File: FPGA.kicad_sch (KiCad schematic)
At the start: 14 parts, among them U3 XC7A100T-FTG256, U5 S25FL127S

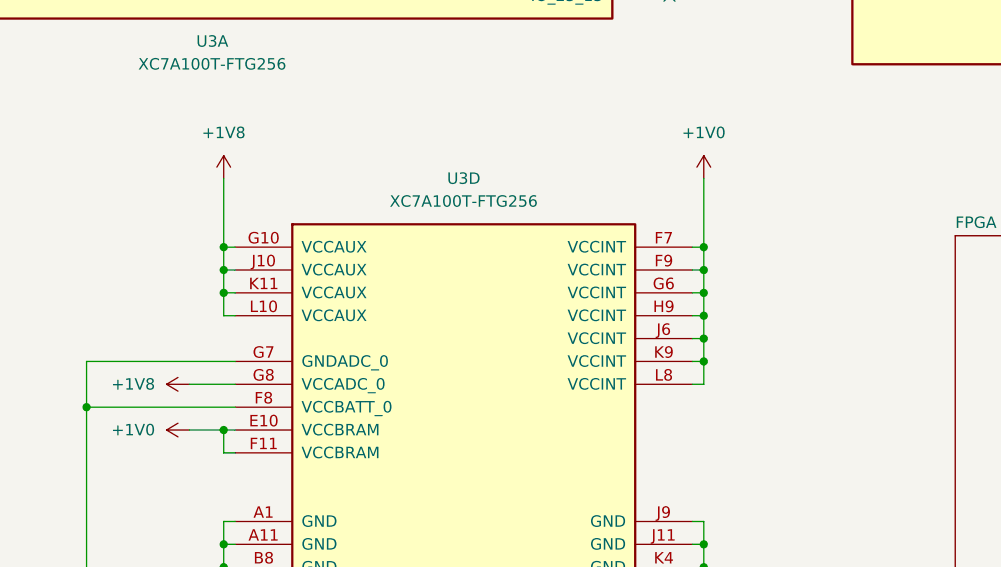
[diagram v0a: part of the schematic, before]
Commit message: Resolved some Electrial Rules
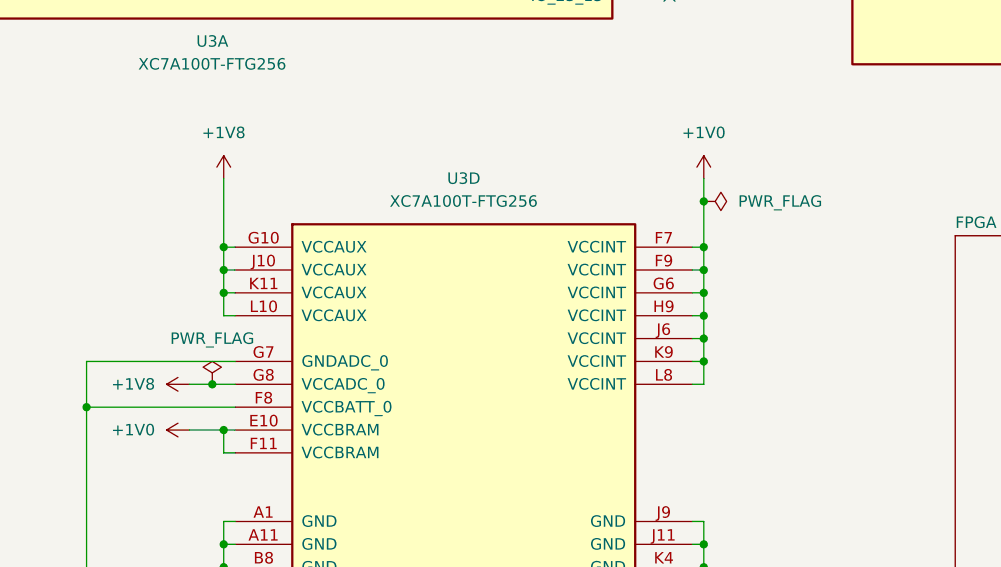
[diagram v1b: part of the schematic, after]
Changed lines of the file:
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@@
   (junction (at 236.22 204.47) (diameter 0) (color 0 0 0 0)
   )
+  (junction (at 289.56 196.85) (diameter 0) (color 0 0 0 0)
+  )
   (junction (at 109.22 182.88) (diameter 0) (color 0 0 0 0)
   )
@@
   )
   (junction (at 236.22 237.49) (diameter 0) (color 0 0 0 0)
+  )
+  (junction (at 234.95 217.17) (diameter 0) (color 0 0 0 0)
   )
   (junction (at 312.42 29.21) (diameter 0) (color 0 0 0 0)
@@
     (stroke (width 0) (type default))
   )
+  (wire (pts (xy 289.56 196.85) (xy 289.56 201.93))
+    (stroke (width 0) (type default))
+  )
   (wire (pts (xy 66.04 78.74) (xy 66.04 81.28))
     (stroke (width 0) (type default))
@@
     (stroke (width 0) (type default))
   )
+  (wire (pts (xy 234.95 217.17) (xy 237.49 217.17))
+    (stroke (width 0) (type default))
+  )
   (wire (pts (xy 236.22 267.97) (xy 237.49 267.97))
     (stroke (width 0) (type default))
@@
     (stroke (width 0) (type default))
   )
-  (wire (pts (xy 232.41 217.17) (xy 237.49 217.17))
+  (wire (pts (xy 232.41 217.17) (xy 234.95 217.17))
     (stroke (width 0) (type default))
   )
@@
     (stroke (width 0) (type default))
   )
-  (wire (pts (xy 289.56 194.31) (xy 289.56 201.93))
+  (wire (pts (xy 289.56 194.31) (xy 289.56 196.85))
     (stroke (width 0) (type default))
   )
@@
     )
   )
+  (symbol (lib_id "power:PWR_FLAG") (at 289.56 196.85 270) (unit 1)
+    (in_bom yes) (on_board yes) (dnp no) (fields_autoplaced)
+    (property "Reference" "#FLG03" (at 291.465 196.85 0)
+      (effects (font (size 1.27 1.27)) hide)
+    )
+    (property "Value" "PWR_FLAG" (at 293.37 196.85 90)
+      (effects (font (size 1.27 1.27)) (justify left))
+    )
+    (property "Footprint" "" (at 289.56 196.85 0)
+      (effects (font (size 1.27 1.27)) hide)
+    )
+    (property "Datasheet" "~" (at 289.56 196.85 0)
+      (effects (font (size 1.27 1.27)) hide)
+    )
+    (pin "1")
+    (instances
+      (project "GuitarZero"
+        (path "/fba50eda-8593-4456-af98-ff56fd418a76/7788bc9b-1e55-4835-b7d3-ea790efb8c61"
+          (reference "#FLG03") (unit 1)
+        )
+      )
+    )
+  )
   (symbol (lib_id "power:+3.3V") (at 90.17 43.18 0) (unit 1)
     (in_bom yes) (on_board yes) (dnp no) (fields_autoplaced)
@@
         )
       )
+    )
+  )
+  (symbol (lib_id "power:PWR_FLAG") (at 234.95 217.17 0) (unit 1)
+    (in_bom yes) (on_board yes) (dnp no) (fields_autoplaced)
+    (property "Reference" "#FLG02" (at 234.95 215.265 0)
+      (effects (font (size 1.27 1.27)) hide)
+    )
+    (property "Value" "PWR_FLAG" (at 234.95 212.09 0)
+      (effects (font (size 1.27 1.27)))
+    )
+    (property "Footprint" "" (at 234.95 217.17 0)
+      (effects (font (size 1.27 1.27)) hide)
+    )
+    (property "Datasheet" "~" (at 234.95 217.17 0)
+      (effects (font (size 1.27 1.27)) hide)
+    )
+    (pin "1")
+    (instances
+      (project "GuitarZero"
+        (path "/fba50eda-8593-4456-af98-ff56fd418a76/7788bc9b-1e55-4835-b7d3-ea790efb8c61"
+          (reference "#FLG02") (unit 1)
+        )
+      )

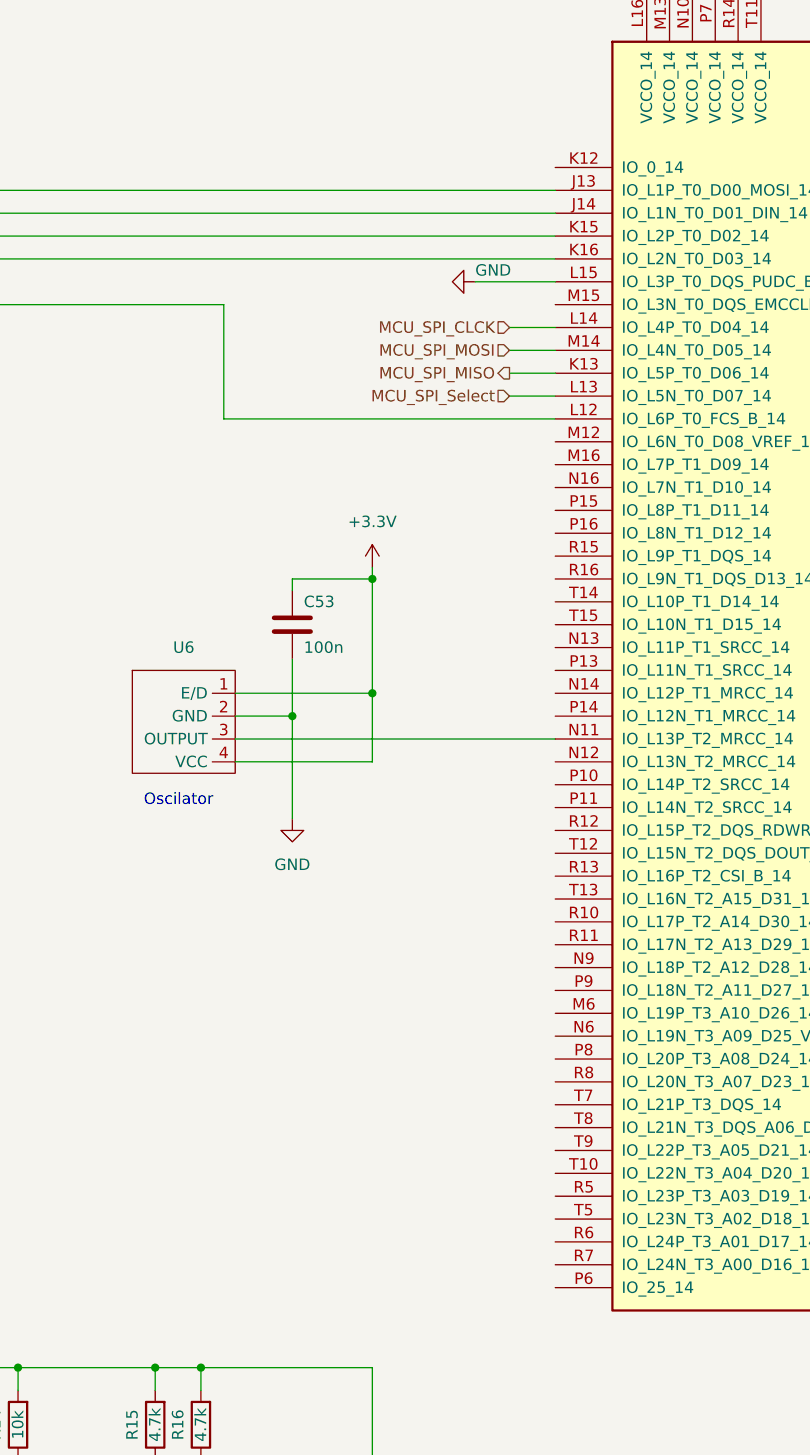
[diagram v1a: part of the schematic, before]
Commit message: Connected FPGA and DAC
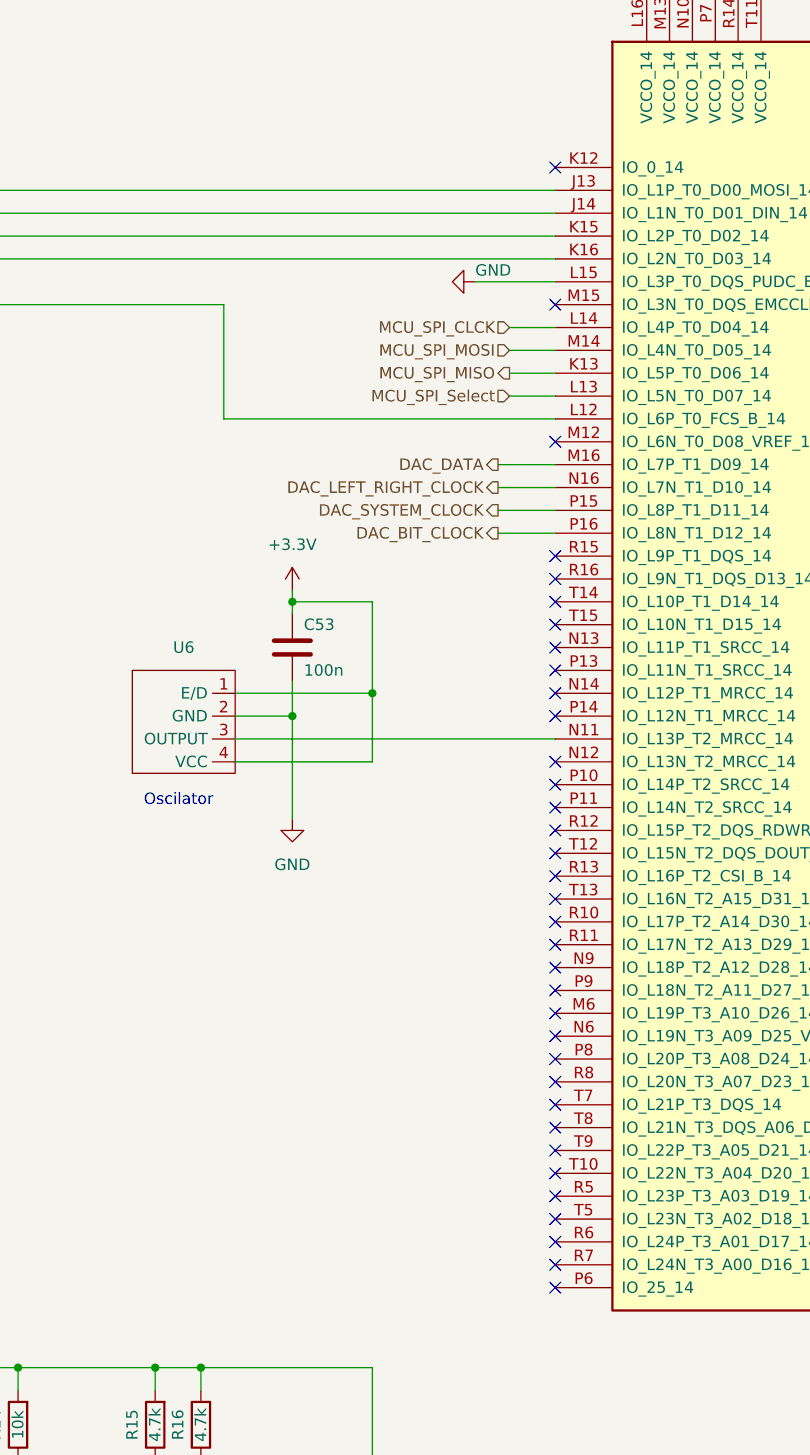
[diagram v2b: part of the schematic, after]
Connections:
- net DAC_DATA: now reaches U3.M16 (IO_L7P_T1_D09_14)
- net DAC_LEFT_RIGHT_CLOCK: now reaches U3.N16 (IO_L7N_T1_D10_14)
- net DAC_SYSTEM_CLOCK: now reaches U3.P15 (IO_L8P_T1_D11_14)
- net DAC_BIT_CLOCK: now reaches U3.P16 (IO_L8N_T1_D12_14)
- no-connect marks 124 -> 159
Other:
- moved on the sheet: C53
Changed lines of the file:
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@@
   (junction (at 236.22 245.11) (diameter 0) (color 0 0 0 0)
   )
-  (junction (at 163.83 95.25) (diameter 0) (color 0 0 0 0)
-  )
   (junction (at 102.87 256.54) (diameter 0) (color 0 0 0 0)
   )
@@
   (junction (at 60.96 64.77) (diameter 0) (color 0 0 0 0)
   )
+  (junction (at 154.94 97.79) (diameter 0) (color 0 0 0 0)
+  )
   (junction (at 289.56 267.97) (diameter 0) (color 0 0 0 0)
   )
@@
   )
   (no_connect (at 285.75 120.65))
+  (no_connect (at 184.15 151.13))
   (no_connect (at 299.72 80.01))
   (no_connect (at 299.72 64.77))
@@
   (no_connect (at 299.72 90.17))
   (no_connect (at 401.32 97.79))
+  (no_connect (at 184.15 140.97))
   (no_connect (at 401.32 161.29))
   (no_connect (at 401.32 57.15))
@@
   (no_connect (at 285.75 74.93))
   (no_connect (at 285.75 110.49))
+  (no_connect (at 184.15 95.25))
   (no_connect (at 401.32 123.19))
   (no_connect (at 401.32 125.73))
@@
   (no_connect (at 401.32 113.03))
   (no_connect (at 285.75 135.89))
+  (no_connect (at 184.15 49.53))
   (no_connect (at 285.75 85.09))
   (no_connect (at 299.72 74.93))
@@
   (no_connect (at 401.32 166.37))
   (no_connect (at 285.75 125.73))
+  (no_connect (at 184.15 107.95))
+  (no_connect (at 184.15 100.33))
   (no_connect (at 401.32 156.21))
   (no_connect (at 285.75 166.37))
@@
   (no_connect (at 285.75 153.67))
   (no_connect (at 401.32 105.41))
+  (no_connect (at 184.15 80.01))
   (no_connect (at 401.32 102.87))
   (no_connect (at 401.32 135.89))
+  (no_connect (at 184.15 158.75))
   (no_connect (at 285.75 156.21))
   (no_connect (at 285.75 123.19))
@@
   (no_connect (at 299.72 87.63))
   (no_connect (at 285.75 133.35))
+  (no_connect (at 184.15 171.45))
   (no_connect (at 285.75 82.55))
+  (no_connect (at 184.15 120.65))
   (no_connect (at 401.32 173.99))
+  (no_connect (at 184.15 102.87))
   (no_connect (at 299.72 85.09))
   (no_connect (at 299.72 77.47))
@@
   (no_connect (at 285.75 118.11))
   (no_connect (at 401.32 163.83))
+  (no_connect (at 184.15 168.91))
   (no_connect (at 285.75 52.07))
   (no_connect (at 285.75 59.69))
   (no_connect (at 285.75 115.57))
   (no_connect (at 285.75 151.13))
+  (no_connect (at 184.15 135.89))
   (no_connect (at 401.32 133.35))
   (no_connect (at 285.75 168.91))
+  (no_connect (at 184.15 173.99))
+  (no_connect (at 184.15 64.77))
   (no_connect (at 299.72 102.87))
   (no_connect (at 285.75 95.25))
   (no_connect (at 285.75 69.85))
+  (no_connect (at 184.15 128.27))
   (no_connect (at 285.75 80.01))
   (no_connect (at 401.32 87.63))
@@
   (no_connect (at 401.32 77.47))
   (no_connect (at 285.75 92.71))
+  (no_connect (at 184.15 97.79))
   (no_connect (at 285.75 140.97))
   (no_connect (at 401.32 110.49))
   (no_connect (at 401.32 128.27))
+  (no_connect (at 184.15 148.59))
+  (no_connect (at 184.15 118.11))
+  (no_connect (at 184.15 146.05))
+  (no_connect (at 184.15 130.81))
+  (no_connect (at 184.15 133.35))
   (no_connect (at 285.75 49.53))
   (no_connect (at 401.32 158.75))
@@
   (no_connect (at 101.6 261.62))
   (no_connect (at 299.72 54.61))
+  (no_connect (at 184.15 123.19))
   (no_connect (at 401.32 146.05))
   (no_connect (at 299.72 67.31))
   (no_connect (at 285.75 100.33))
+  (no_connect (at 184.15 125.73))
   (no_connect (at 285.75 161.29))
   (no_connect (at 285.75 113.03))
   (no_connect (at 401.32 90.17))
+  (no_connect (at 184.15 161.29))
   (no_connect (at 299.72 97.79))
   (no_connect (at 285.75 146.05))
@@
   (no_connect (at 401.32 120.65))
   (no_connect (at 285.75 57.15))
+  (no_connect (at 184.15 163.83))
   (no_connect (at 401.32 143.51))
   (no_connect (at 285.75 105.41))
@@
   (no_connect (at 285.75 107.95))
   (no_connect (at 401.32 100.33))
+  (no_connect (at 184.15 143.51))
   (no_connect (at 401.32 138.43))
   (no_connect (at 101.6 264.16))
   (no_connect (at 401.32 85.09))
+  (no_connect (at 184.15 138.43))
   (no_connect (at 299.72 82.55))
+  (no_connect (at 184.15 92.71))
   (no_connect (at 299.72 95.25))
+  (no_connect (at 184.15 156.21))
+  (no_connect (at 184.15 153.67))
   (no_connect (at 285.75 173.99))
+  (no_connect (at 184.15 166.37))
+  (no_connect (at 184.15 110.49))
+  (no_connect (at 184.15 115.57))
   (no_connect (at 401.32 74.93))
   (no_connect (at 285.75 130.81))
   (no_connect (at 299.72 92.71))
+  (no_connect (at 184.15 105.41))
   (no_connect (at 285.75 77.47))
-  (wire (pts (xy 154.94 95.25) (xy 154.94 96.52))
+  (wire (pts (xy 154.94 96.52) (xy 154.94 97.79))
     (stroke (width 0) (type default))
   )
@@
     (stroke (width 0) (type default))
   )
+  (wire (pts (xy 154.94 97.79) (xy 154.94 99.06))
+    (stroke (width 0) (type default))
+  )
   (wire (pts (xy 179.07 74.93) (xy 184.15 74.93))
     (stroke (width 0) (type default))
@@
     (stroke (width 0) (type default))
   )
+  (wire (pts (xy 177.8 85.09) (xy 184.15 85.09))
+    (stroke (width 0) (type default))
+  )
   (wire (pts (xy 102.87 248.92) (xy 102.87 254))
     (stroke (width 0) (type default))
@@
     (stroke (width 0) (type default))
   )
-  (wire (pts (xy 163.83 95.25) (xy 163.83 107.95))
+  (wire (pts (xy 163.83 97.79) (xy 163.83 107.95))
     (stroke (width 0) (type default))
   )
@@
     (stroke (width 0) (type default))
   )
-  (wire (pts (xy 163.83 93.98) (xy 163.83 95.25))
-    (stroke (width 0) (type default))
-  )
   (wire (pts (xy 147.32 77.47) (xy 184.15 77.47))
     (stroke (width 0) (type default))
@@
     (stroke (width 0) (type default))
   )
+  (wire (pts (xy 177.8 90.17) (xy 184.15 90.17))
+    (stroke (width 0) (type default))
+  )
   (wire (pts (xy 349.25 29.21) (xy 349.25 33.02))
     (stroke (width 0) (type default))
@@
     (stroke (width 0) (type default))
   )
+  (wire (pts (xy 154.94 97.79) (xy 163.83 97.79))
+    (stroke (width 0) (type default))
+  )
   (wire (pts (xy 60.96 71.12) (xy 68.58 71.12))
     (stroke (width 0) (type default))
@@
     (stroke (width 0) (type default))
   )
-  (wire (pts (xy 154.94 104.14) (xy 154.94 110.49))
+  (wire (pts (xy 154.94 106.68) (xy 154.94 110.49))
     (stroke (width 0) (type default))
   )
@@
     (stroke (width 0) (type default))
   )
-  (wire (pts (xy 154.94 95.25) (xy 163.83 95.25))
-    (stroke (width 0) (type default))
-  )
   (wire (pts (xy 289.56 255.27) (xy 289.56 257.81))
     (stroke (width 0) (type default))
@@
     (stroke (width 0) (type default))
   )
+  (wire (pts (xy 177.8 87.63) (xy 184.15 87.63))
+    (stroke (width 0) (type default))
+  )
   (wire (pts (xy 105.41 256.54) (xy 105.41 259.08))
     (stroke (width 0) (type default))
@@
   )
   (wire (pts (xy 289.56 232.41) (xy 288.29 232.41))
+    (stroke (width 0) (type default))
+  )
+  (wire (pts (xy 177.8 82.55) (xy 184.15 82.55))
     (stroke (width 0) (type default))
   )
@@
     (effects (font (size 1.27 1.27)) (justify left bottom))
   )
+  (hierarchical_label "DAC_BIT_CLOCK" (shape output) (at 177.8 90.17 180) (fields_autoplaced)
+    (effects (font (size 1.27 1.27)) (justify right))
+  )
+  (hierarchical_label "DAC_SYSTEM_CLOCK" (shape output) (at 177.8 87.63 180) (fields_autoplaced)
+    (effects (font (size 1.27 1.27)) (justify right))
+  )
   (hierarchical_label "MCU_SPI_MISO" (shape output) (at 179.07 72.39 180) (fields_autoplaced)
     (effects (font (size 1.27 1.27)) (justify right))
   )
+  (hierarchical_label "DAC_LEFT_RIGHT_CLOCK" (shape output) (at 177.8 85.09 180) (fields_autoplaced)
+    (effects (font (size 1.27 1.27)) (justify right))
+  )
   (hierarchical_label "MCU_SPI_MOSI" (shape input) (at 179.07 69.85 180) (fields_autoplaced)
     (effects (font (size 1.27 1.27)) (justify right))
   )
+  (hierarchical_label "DAC_DATA" (shape output) (at 177.8 82.55 180) (fields_autoplaced)
+    (effects (font (size 1.27 1.27)) (justify right))
+  )
   (hierarchical_label "Done" (shape output) (at 106.68 229.87 90) (fields_autoplaced)
     (effects (font (size 1.27 1.27)) (justify left))
@@
     (effects (font (size 1.27 1.27)) (justify right))
   )
-  (symbol (lib_id "Device:C") (at 154.94 100.33 0) (unit 1)
+  (symbol (lib_id "Device:C") (at 154.94 102.87 0) (unit 1)
     (in_bom yes) (on_board yes) (dnp no)
-    (property "Reference" "C53" (at 156.21 97.79 0)
+    (property "Reference" "C53" (at 156.21 100.33 0)
       (effects (font (size 1.27 1.27)) (justify left))
     )
-    (property "Value" "100n" (at 156.21 102.87 0)
+    (property "Value" "100n" (at 156.21 105.41 0)
       (effects (font (size 1.27 1.27)) (justify left))
     )
-    (property "Footprint" "" (at 155.9052 104.14 0)
-      (effects (font (size 1.27 1.27)) hide)
-    )
-    (property "Datasheet" "~" (at 154.94 100.33 0)
+    (property "Footprint" "" (at 155.9052 106.68 0)
+      (effects (font (size 1.27 1.27)) hide)
+    )
+    (property "Datasheet" "~" (at 154.94 102.87 0)
       (effects (font (size 1.27 1.27)) hide)
     )
@@
     )
   )
-  (symbol (lib_id "power:+3.3V") (at 163.83 93.98 0) (unit 1)
+  (symbol (lib_id "power:+3.3V") (at 154.94 96.52 0) (unit 1)
     (in_bom yes) (on_board yes) (dnp no) (fields_autoplaced)
-    (property "Reference" "#PWR026" (at 163.83 97.79 0)
-      (effects (font (size 1.27 1.27)) hide)
-    )
-    (property "Value" "+3.3V" (at 163.83 88.9 0)
+    (property "Reference" "#PWR026" (at 154.94 100.33 0)
+      (effects (font (size 1.27 1.27)) hide)
+    )
+    (property "Value" "+3.3V" (at 154.94 91.44 0)
       (effects (font (size 1.27 1.27)))
     )
-    (property "Footprint" "" (at 163.83 93.98 0)
-      (effects (font (size 1.27 1.27)) hide)
-    )
-    (property "Datasheet" "" (at 163.83 93.98 0)
-      (effects (font (size 1.27 1.27)) hide)
-    )
+    (property "Footprint" "" (at 154.94 96.52 0)
+      (effects (font (size 1.27 1.27)) hide)
+    )
+    (property "Datasheet" "" (at 154.94 96.52 0)
+      (effects (font (size 1.27 1.27)) hide)
+    )
